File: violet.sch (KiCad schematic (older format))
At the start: 38 parts, among them J1 NEIGHBOR1, J2 NEIGHBOR2, J3 NEIGHBOR1, J4 BONUS_ROW, J5 NEIGHBOR2, J6 NEIGHBOR1, J7 BONUS_ROW, J8 BONUS_ROW, J9 NEIGHBOR2, U1 PCA9698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

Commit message: Remove U3 & U4; re-label signals; set up U5; fix U1 &U2 I2C addresses; fix minor errors
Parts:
- removed C10: C, symbol Device:C
- removed C9: 100nF, gsg-modules:0603, symbol Device:C
- removed U3: PCA9674, gsg-modules:TSSOP16, symbol gsg-symbols:PCA9674
- removed U4: 74HC4051, symbol 74xx:74HC4051
- C7, C8: value C -> 1uF; Description (none) -> CAP CER 1UF 10V X5R 0603; Manufacturer (none) -> Samsung Electro-Mechanics; Part Number (none) -> CL10A105KP8NNNC
- R10: value R -> 0.1; footprint (none) -> gsg-modules:0603; Description (none) -> RES 0.1 OHM 1% 1/10W 0603; Manufacturer (none) -> Panasonic Electronic Components; Part Number (none) -> ERJ-3RSFR10V
- R8: value R -> 12k; footprint (none) -> gsg-modules:0603; Description (none) -> RES 12K OHM 1% 1/10W 0603; Manufacturer (none) -> Stackpole; Part Number (none) -> RMCF0603FT12K0
- R9: value R -> 43.2k; footprint (none) -> gsg-modules:0603; Description (none) -> RES SMD 43.2K OHM 1% 1/10W 0603; Manufacturer (none) -> Yageo; Part Number (none) -> RC0603FR-0743K2L
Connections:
- net EUT_5V is gone; now on net ADC0_5: U5.6 (VOUT)
- net U3_IO_P0 is gone; now on net U1_IO2_7: J5.30 (Pin_30)
- net U3_IO_P1 is gone; now on net U1_IO2_6: J5.32 (Pin_32)
- net U3_IO_P2 is gone; now on net U1_IO2_5: J5.38 (Pin_38)
- net U3_IO_P3 is gone; now on net U1_IO2_3: J4.11 (Pin_11)
- net U3_IO_P4 is gone; now on net U1_IO2_4: J5.2 (Pin_2)
- net +5V: no longer C8.1, U5.1 (VIN)
- net ADC0_2: now also J3.2 (Pin_2), R10.1; no longer J4.5 (Pin_5), J8.5 (Pin_5)
- net ADC0_5: now also C7.1, R10.2; no longer J4.4 (Pin_4), J8.4 (Pin_4)
- net EUT_P1_10: now also J3.20 (Pin_20)
- net EUT_P1_11: now also J3.22 (Pin_22)
- net EUT_P1_12: now also J3.21 (Pin_21)
- net EUT_P1_13: now also J3.26 (Pin_26)
- net EUT_P1_14: now also J3.25 (Pin_25)
- net EUT_P1_7: now also J3.15 (Pin_15)
- net EUT_P1_8: now also J3.18 (Pin_18)
- net EUT_P1_9: now also J3.17 (Pin_17)
- net GND: now also C7.2, R7.2; no longer C7.1, R8.2
- net I2C0_SCL: now also U1.28 (AD1), U2.28 (AD1); no longer J5.40 (Pin_40), J9.40 (Pin_40)
- net I2C0_SDA: no longer J5.39 (Pin_39), J9.39 (Pin_39)
- net P1_15: no longer R7.2
- net P1_5: no longer J6.13 (Pin_13)
- net P1_6: no longer J6.16 (Pin_16)
- net P2_3: no longer J9.20 (Pin_20)
- net P2_5: no longer J9.18 (Pin_18)
- net P4_2: now also R7.1; no longer J9.8 (Pin_8), R8.1
- net P4_6: now also R8.2; no longer R10.2
- net P5_0: no longer J6.8 (Pin_8)
- net P5_2: no longer J6.14 (Pin_14)
- net P5_3: no longer J6.19 (Pin_19)
- net P5_4: no longer J6.24 (Pin_24)
- net P5_5: no longer J6.23 (Pin_23)
- net P5_6: no longer J6.27 (Pin_27)
- net P6_8: no longer J9.29 (Pin_29)
- net P7_0: no longer J9.27 (Pin_27)
- net U1_IO0_2: no longer U1.5 (IO0_2)
- net U1_IO2_3: no longer J3.27 (Pin_27)
- net U1_IO2_4: no longer J3.26 (Pin_26)
- net U1_IO2_5: no longer J3.25 (Pin_25)
- net U1_IO2_6: no longer J3.24 (Pin_24)
- net U1_IO2_7: no longer J3.23 (Pin_23)
- net VCC: now also C8.1, R8.1, U5.1 (VIN); no longer C7.2, J3.2 (Pin_2), J6.2 (Pin_2), R10.1, R7.1, U1.28 (AD1), U2.28 (AD1)
- removed net U1_IO3_0: J3.22 (Pin_22), U1.36 (IO3_0), U2.36 (IO3_0)
- net U1_IO3_1: no longer names the net of U1.37 (IO3_1)
- net U1_IO3_1: no longer J3.21 (Pin_21)
- net U1_IO3_2: no longer names the net of U1.38 (IO3_2)
- net U1_IO3_2: no longer J3.20 (Pin_20)
- net U1_IO3_3: no longer names the net of U1.40 (IO3_3)
- net U1_IO3_3: no longer J3.19 (Pin_19)
- net U1_IO3_4: no longer names the net of U1.41 (IO3_4)
- net U1_IO3_4: no longer J3.18 (Pin_18)
- net U1_IO3_5: no longer names the net of U1.42 (IO3_5)
- net U1_IO3_5: no longer J3.17 (Pin_17)
- net U1_IO3_6: no longer names the net of U1.43 (IO3_6)
- net U1_IO3_6: no longer J3.16 (Pin_16)
- net U1_IO3_7: no longer names the net of U1.44 (IO3_7)
- net U1_IO3_7: no longer J3.15 (Pin_15)
- net U1_IO4_0: no longer names the net of U1.45 (IO4_0)
- net U1_IO4_0: no longer J3.14 (Pin_14)
- net U1_IO4_1: no longer names the net of U1.47 (IO4_1)
- net U1_IO4_1: no longer J3.13 (Pin_13)
- net U1_IO4_5: no longer names the net of U1.52 (IO4_5)
- net U1_IO4_5: no longer J3.8 (Pin_8)
- net U2_IO3_0 renamed EUT_P4_2
- net EUT_P4_2: now also J9.8 (Pin_8)
- net U2_IO4_0: no longer names the net of U2.45 (IO4_0)
- net U2_IO4_0: no longer J5.18 (Pin_18)
- net U2_IO4_2: no longer names the net of U2.48 (IO4_2)
- net U2_IO4_2: no longer J5.20 (Pin_20)
- net U2_IO4_6: no longer names the net of U2.53 (IO4_6)
- net U2_IO4_6: no longer J5.27 (Pin_27)
- net U2_IO4_7: no longer names the net of U2.54 (IO4_7)
- net U2_IO4_7: no longer J5.29 (Pin_29)
- new net EUT_ADC0_2: J4.5 (Pin_5), J8.5 (Pin_5)
- new net EUT_ADC0_5: J4.4 (Pin_4), J8.4 (Pin_4)
- new net EUT_I2C0_SCL: J5.40 (Pin_40), J9.40 (Pin_40)
- new net EUT_I2C0_SDA: J5.39 (Pin_39), J9.39 (Pin_39)
- new net EUT_P1_5: J3.13 (Pin_13), J6.13 (Pin_13)
- new net EUT_P1_6: J3.16 (Pin_16), J6.16 (Pin_16)
- new net EUT_P2_3: J5.20 (Pin_20), J9.20 (Pin_20)
- new net EUT_P2_5: J5.18 (Pin_18), J9.18 (Pin_18)
- new net EUT_P5_0: J3.8 (Pin_8), J6.8 (Pin_8)
- new net EUT_P5_2: J3.14 (Pin_14), J6.14 (Pin_14)
- new net EUT_P5_3: J3.19 (Pin_19), J6.19 (Pin_19)
- new net EUT_P5_4: J3.24 (Pin_24), J6.24 (Pin_24)
- new net EUT_P5_5: J3.23 (Pin_23), J6.23 (Pin_23)
- new net EUT_P5_6: J3.27 (Pin_27), J6.27 (Pin_27)
- new net EUT_P6_8: J5.29 (Pin_29), J9.29 (Pin_29)
- new net EUT_P7_0: J5.27 (Pin_27), J9.27 (Pin_27)
- no-connect marks 168 -> 162
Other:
- note added: "Address: 0x10"
- note added: "Address: 0x11"
- note added: "Plug Gladiolus/Azalea testing unit in here."
- note removed: "???"
- note removed: "Plug Gladiolus testing unit in here."
- moved on the sheet: C8, R9, U5

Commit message: Add remaining footprints
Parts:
- added J10: Conn_01x08, gsg-modules:HEADER-1x8, symbol Connector_Generic:Conn_01x08
- C7, C8: footprint (none) -> gsg-modules:0603
- J1, J2, J3, J5, J6, J9: footprint neighbor:HEADER-2x20 -> gsg-modules:HEADER-2x20
- J4, J7, J8: footprint neighbor:HEADER-1x20 -> gsg-modules:HEADER-1x20
- U5: footprint (none) -> gsg-modules:SOT457
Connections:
- no-connect marks 162 -> 170
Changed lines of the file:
@@
 F 0 "J2" H 15500 2900 50  0000 C CNN
 F 1 "NEIGHBOR2" V 15500 1850 50  0000 C CNN
-F 2 "neighbor:HEADER-2x20" H 15450 900 60  0001 C CNN
+F 2 "gsg-modules:HEADER-2x20" H 15450 900 60  0001 C CNN
 F 3 "" H 15450 900 60  0000 C CNN
 F 4 "Adam Tech" H 15450 1850 60  0001 C CNN "Manufacturer"
@@
 F 0 "J1" H 13800 2900 50  0000 C CNN
 F 1 "NEIGHBOR1" V 13800 1850 50  0000 C CNN
-F 2 "neighbor:HEADER-2x20" H 13750 900 60  0001 C CNN
+F 2 "gsg-modules:HEADER-2x20" H 13750 900 60  0001 C CNN
 F 3 "" H 13750 900 60  0000 C CNN
 F 4 "Adam Tech" H 13750 1850 60  0001 C CNN "Manufacturer"
@@
 F 0 "J7" H 14600 4300 50  0000 C CNN
 F 1 "BONUS_ROW" V 14700 3250 50  0000 C CNN
-F 2 "neighbor:HEADER-1x20" H 14600 3250 60  0001 C CNN
+F 2 "gsg-modules:HEADER-1x20" H 14600 3250 60  0001 C CNN
 F 3 "" H 14600 3250 60  0000 C CNN
 F 4 "Samtec" H 14600 3250 60  0001 C CNN "Manufacturer"
@@
 F 0 "J5" H 3850 3400 50  0000 C CNN
 F 1 "NEIGHBOR2" V 3850 2350 50  0000 C CNN
-F 2 "neighbor:HEADER-2x20" H 3800 1400 60  0001 C CNN
+F 2 "gsg-modules:HEADER-2x20" H 3800 1400 60  0001 C CNN
 F 3 "" H 3800 1400 60  0000 C CNN
 F 4 "Adam Tech" H 3800 2350 60  0001 C CNN "Manufacturer"
@@
 F 0 "J3" H 2150 3400 50  0000 C CNN
 F 1 "NEIGHBOR1" V 2150 2350 50  0000 C CNN
-F 2 "neighbor:HEADER-2x20" H 2100 1400 60  0001 C CNN
+F 2 "gsg-modules:HEADER-2x20" H 2100 1400 60  0001 C CNN
 F 3 "" H 2100 1400 60  0000 C CNN
 F 4 "Adam Tech" H 2100 2350 60  0001 C CNN "Manufacturer"
@@
 F 0 "J4" H 2950 4800 50  0000 C CNN
 F 1 "BONUS_ROW" V 3050 3750 50  0000 C CNN
-F 2 "neighbor:HEADER-1x20" H 2950 3750 60  0001 C CNN
+F 2 "gsg-modules:HEADER-1x20" H 2950 3750 60  0001 C CNN
 F 3 "" H 2950 3750 60  0000 C CNN
 F 4 "Samtec" H 2950 3750 60  0001 C CNN "Manufacturer"
@@
 F 0 "U5" H 7500 7337 60  0000 C CNN
 F 1 "AP2553W6-7" H 7500 7231 60  0000 C CNN
-F 2 "" H 7500 6950 60  0000 C CNN
+F 2 "gsg-modules:SOT457" H 7500 6950 60  0001 C CNN
 F 3 "" H 7500 6950 60  0000 C CNN
 	1    7500 6950
@@
 F 0 "C8" H 6365 7096 50  0000 L CNN
 F 1 "1uF" H 6365 7005 50  0000 L CNN
-F 2 "" H 6288 6900 50  0001 C CNN
+F 2 "gsg-modules:0603" H 6288 6900 50  0001 C CNN
 F 3 "~" H 6250 7050 50  0001 C CNN
 F 4 "Samsung Electro-Mechanics" H 6250 7050 50  0001 C CNN "Manufacturer"
@@
 F 0 "J9" H 15550 8050 50  0000 C CNN
 F 1 "NEIGHBOR2" V 15550 7000 50  0000 C CNN
-F 2 "neighbor:HEADER-2x20" H 15500 6050 60  0001 C CNN
+F 2 "gsg-modules:HEADER-2x20" H 15500 6050 60  0001 C CNN
 F 3 "" H 15500 6050 60  0000 C CNN
 F 4 "Adam Tech" H 15500 7000 60  0001 C CNN "Manufacturer"
@@
 F 0 "J6" H 13850 8050 50  0000 C CNN
 F 1 "NEIGHBOR1" V 13850 7000 50  0000 C CNN
-F 2 "neighbor:HEADER-2x20" H 13800 6050 60  0001 C CNN
+F 2 "gsg-modules:HEADER-2x20" H 13800 6050 60  0001 C CNN
 F 3 "" H 13800 6050 60  0000 C CNN
 F 4 "Adam Tech" H 13800 7000 60  0001 C CNN "Manufacturer"
@@
 F 0 "J8" H 14050 9400 50  0000 C CNN
 F 1 "BONUS_ROW" V 14150 8350 50  0000 C CNN
-F 2 "neighbor:HEADER-1x20" H 14050 8350 60  0001 C CNN
+F 2 "gsg-modules:HEADER-1x20" H 14050 8350 60  0001 C CNN
 F 3 "" H 14050 8350 60  0000 C CNN
 F 4 "Samtec" H 14050 8350 60  0001 C CNN "Manufacturer"
@@
 F 0 "C7" H 9015 7146 50  0000 L CNN
 F 1 "1uF" H 9015 7055 50  0000 L CNN
-F 2 "" H 8938 6950 50  0001 C CNN
+F 2 "gsg-modules:0603" H 8938 6950 50  0001 C CNN
 F 3 "~" H 8900 7100 50  0001 C CNN
 F 4 "Samsung Electro-Mechanics" H 8900 7100 50  0001 C CNN "Manufacturer"
@@
 NoConn ~ 5600 1950
 NoConn ~ 14250 2250
+$Comp
+L Connector_Generic:Conn_01x08 J10
+U 1 1 605A089F
+P 2050 6150
+F 0 "J10" H 2130 6142 50  0000 L CNN
+F 1 "Conn_01x08" H 2130 6051 50  0000 L CNN
+F 2 "gsg-modules:HEADER-1x8" H 2050 6150 50  0001 C CNN
+F 3 "~" H 2050 6150 50  0001 C CNN
+F 4 "Samtec Inc." H 2050 6150 50  0001 C CNN "Manufacturer"
+F 5 "SSQ-108-01-G-S" H 2050 6150 50  0001 C CNN "Part Number"
+F 6 "CONN RCPT 8POS 0.1 GOLD PCB" H 2050 6150 50  0001 C CNN "Description"
+	1    2050 6150
+	1    0    0    -1
+$EndComp
+NoConn ~ 1850 5850
+NoConn ~ 1850 5950
+NoConn ~ 1850 6050
+NoConn ~ 1850 6150
+NoConn ~ 1850 6250
+NoConn ~ 1850 6350
+NoConn ~ 1850 6450
+NoConn ~ 1850 6550
 $EndSCHEMATC

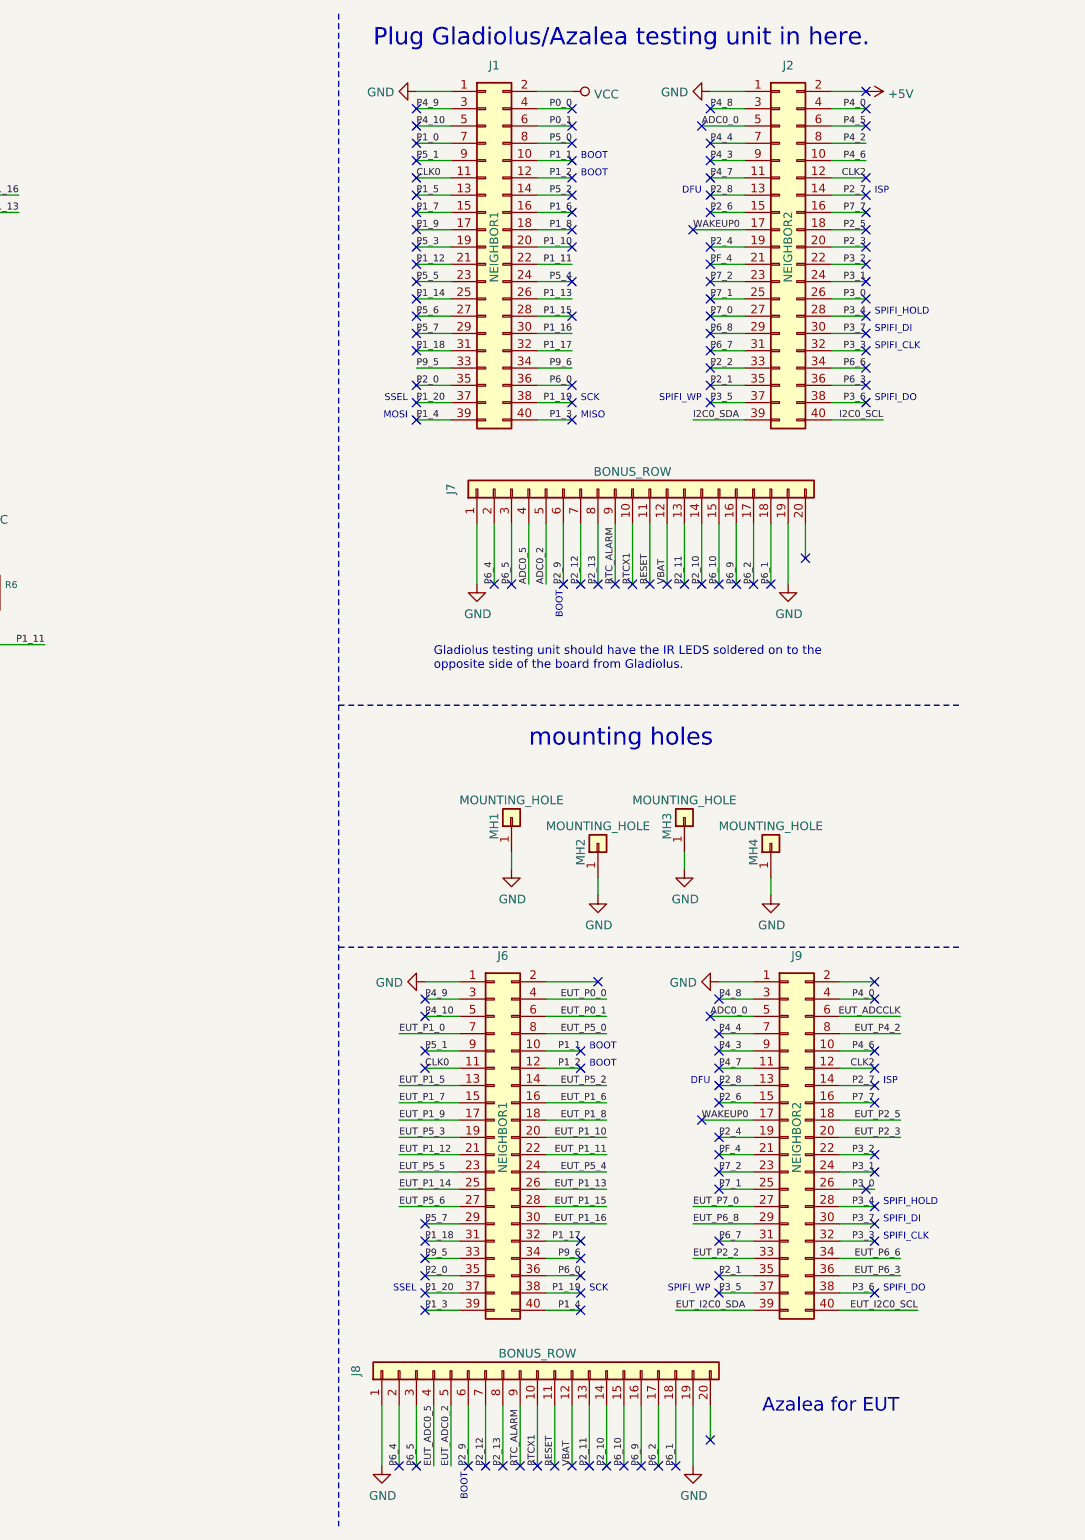
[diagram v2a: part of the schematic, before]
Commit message: Add more mounting holes
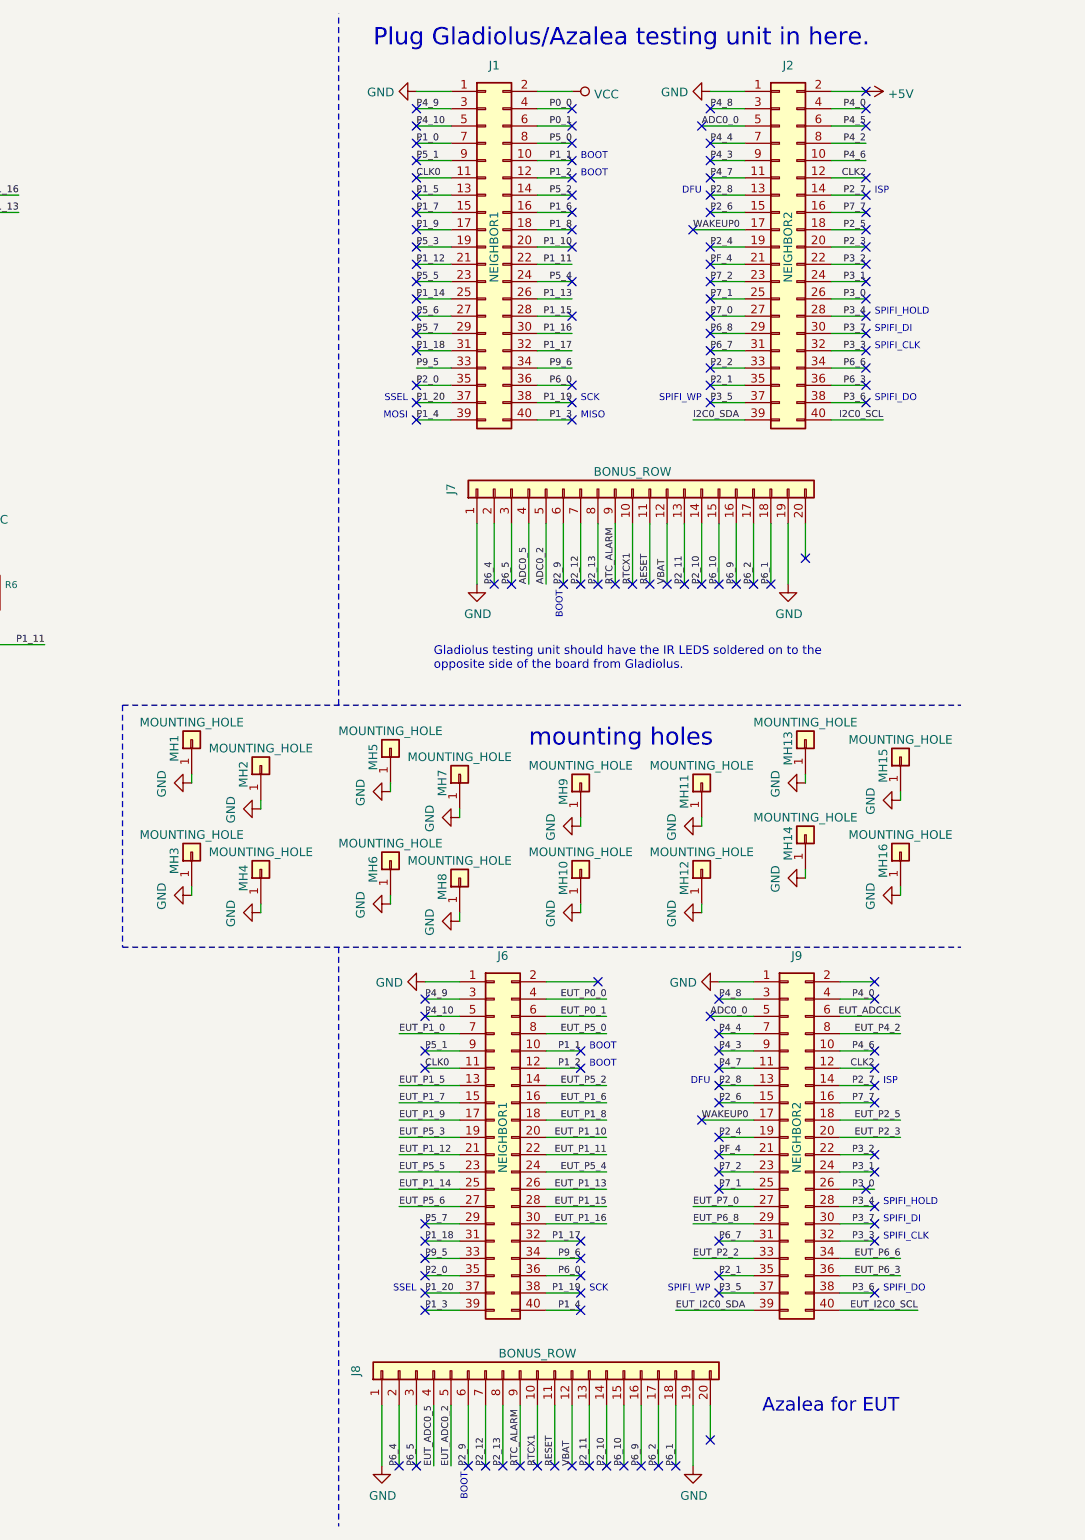
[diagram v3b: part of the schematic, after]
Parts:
- added MH10, MH11, MH12, MH13, MH14, MH15, MH16, MH5, MH6, MH7, MH8, MH9: MOUNTING_HOLE, neighbor:HOLE126MIL-COPPER, symbol Connector_Generic:Conn_01x01
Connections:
- net GND: now also MH10.1 (Pin_1), MH11.1 (Pin_1), MH12.1 (Pin_1), MH13.1 (Pin_1), MH14.1 (Pin_1), MH15.1 (Pin_1), MH16.1 (Pin_1), MH5.1 (Pin_1), MH6.1 (Pin_1), MH7.1 (Pin_1), MH8.1 (Pin_1), MH9.1 (Pin_1)
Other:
- moved on the sheet: MH1, MH2, MH3, MH4

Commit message: Fix mounting hole footprints
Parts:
- MH1, MH10, MH11, MH12, MH13, MH14, MH15, MH16, MH2, MH3, MH4, MH5, MH6, MH7, MH8, MH9: footprint neighbor:HOLE126MIL-COPPER -> gsg-modules:HOLE126MIL-COPPER
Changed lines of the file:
@@
 F 0 "MH3" H 12000 5450 50  0000 C CNN
 F 1 "MOUNTING_HOLE" V 12150 5350 50  0000 C CNN
-F 2 "neighbor:HOLE126MIL-COPPER" H 12050 5350 60  0001 C CNN
+F 2 "gsg-modules:HOLE126MIL-COPPER" H 12050 5350 60  0001 C CNN
 F 3 "" H 12050 5350 60  0000 C CNN
 F 4 "DNP" H 12050 5350 60  0001 C CNN "Note"
@@
 F 0 "MH4" H 12400 5550 50  0000 C CNN
 F 1 "MOUNTING_HOLE" V 12550 5450 50  0000 C CNN
-F 2 "neighbor:HOLE126MIL-COPPER" H 12450 5450 60  0001 C CNN
+F 2 "gsg-modules:HOLE126MIL-COPPER" H 12450 5450 60  0001 C CNN
 F 3 "" H 12450 5450 60  0000 C CNN
 F 4 "DNP" H 12450 5450 60  0001 C CNN "Note"
@@
 F 0 "MH1" H 12000 4800 50  0000 C CNN
 F 1 "MOUNTING_HOLE" V 12150 4700 50  0000 C CNN
-F 2 "neighbor:HOLE126MIL-COPPER" H 12050 4700 60  0001 C CNN
+F 2 "gsg-modules:HOLE126MIL-COPPER" H 12050 4700 60  0001 C CNN
 F 3 "" H 12050 4700 60  0000 C CNN
 F 4 "DNP" H 12050 4700 60  0001 C CNN "Note"
@@
 F 0 "MH2" H 12400 4950 50  0000 C CNN
 F 1 "MOUNTING_HOLE" V 12550 4850 50  0000 C CNN
-F 2 "neighbor:HOLE126MIL-COPPER" H 12450 4850 60  0001 C CNN
+F 2 "gsg-modules:HOLE126MIL-COPPER" H 12450 4850 60  0001 C CNN
 F 3 "" H 12450 4850 60  0000 C CNN
 F 4 "DNP" H 12450 4850 60  0001 C CNN "Note"
@@
 F 0 "MH9" H 14250 5050 50  0000 C CNN
 F 1 "MOUNTING_HOLE" V 14400 4950 50  0000 C CNN
-F 2 "neighbor:HOLE126MIL-COPPER" H 14300 4950 60  0001 C CNN
+F 2 "gsg-modules:HOLE126MIL-COPPER" H 14300 4950 60  0001 C CNN
 F 3 "" H 14300 4950 60  0000 C CNN
 F 4 "DNP" H 14300 4950 60  0001 C CNN "Note"
@@
 F 0 "MH10" H 14250 5550 50  0000 C CNN
 F 1 "MOUNTING_HOLE" V 14400 5450 50  0000 C CNN
-F 2 "neighbor:HOLE126MIL-COPPER" H 14300 5450 60  0001 C CNN
+F 2 "gsg-modules:HOLE126MIL-COPPER" H 14300 5450 60  0001 C CNN
 F 3 "" H 14300 5450 60  0000 C CNN
 F 4 "DNP" H 14300 5450 60  0001 C CNN "Note"
@@
 F 0 "MH11" H 14950 5050 50  0000 C CNN
 F 1 "MOUNTING_HOLE" V 15100 4950 50  0000 C CNN
-F 2 "neighbor:HOLE126MIL-COPPER" H 15000 4950 60  0001 C CNN
+F 2 "gsg-modules:HOLE126MIL-COPPER" H 15000 4950 60  0001 C CNN
 F 3 "" H 15000 4950 60  0000 C CNN
 F 4 "DNP" H 15000 4950 60  0001 C CNN "Note"
@@
 F 0 "MH12" H 14950 5550 50  0000 C CNN
 F 1 "MOUNTING_HOLE" V 15100 5450 50  0000 C CNN
-F 2 "neighbor:HOLE126MIL-COPPER" H 15000 5450 60  0001 C CNN
+F 2 "gsg-modules:HOLE126MIL-COPPER" H 15000 5450 60  0001 C CNN
 F 3 "" H 15000 5450 60  0000 C CNN
 F 4 "DNP" H 15000 5450 60  0001 C CNN "Note"
@@
 F 0 "MH13" H 15550 4800 50  0000 C CNN
 F 1 "MOUNTING_HOLE" V 15700 4700 50  0000 C CNN
-F 2 "neighbor:HOLE126MIL-COPPER" H 15600 4700 60  0001 C CNN
+F 2 "gsg-modules:HOLE126MIL-COPPER" H 15600 4700 60  0001 C CNN
 F 3 "" H 15600 4700 60  0000 C CNN
 F 4 "DNP" H 15600 4700 60  0001 C CNN "Note"
@@
 F 0 "MH14" H 15550 5350 50  0000 C CNN
 F 1 "MOUNTING_HOLE" V 15700 5250 50  0000 C CNN
-F 2 "neighbor:HOLE126MIL-COPPER" H 15600 5250 60  0001 C CNN
+F 2 "gsg-modules:HOLE126MIL-COPPER" H 15600 5250 60  0001 C CNN
 F 3 "" H 15600 5250 60  0000 C CNN
 F 4 "DNP" H 15600 5250 60  0001 C CNN "Note"
@@
 F 0 "MH15" H 16100 4900 50  0000 C CNN
 F 1 "MOUNTING_HOLE" V 16250 4800 50  0000 C CNN
-F 2 "neighbor:HOLE126MIL-COPPER" H 16150 4800 60  0001 C CNN
+F 2 "gsg-modules:HOLE126MIL-COPPER" H 16150 4800 60  0001 C CNN
 F 3 "" H 16150 4800 60  0000 C CNN
 F 4 "DNP" H 16150 4800 60  0001 C CNN "Note"
@@
 F 0 "MH16" H 16100 5450 50  0000 C CNN
 F 1 "MOUNTING_HOLE" V 16250 5350 50  0000 C CNN
-F 2 "neighbor:HOLE126MIL-COPPER" H 16150 5350 60  0001 C CNN
+F 2 "gsg-modules:HOLE126MIL-COPPER" H 16150 5350 60  0001 C CNN
 F 3 "" H 16150 5350 60  0000 C CNN
 F 4 "DNP" H 16150 5350 60  0001 C CNN "Note"
@@
 F 0 "MH6" H 13150 5500 50  0000 C CNN
 F 1 "MOUNTING_HOLE" V 13300 5400 50  0000 C CNN
-F 2 "neighbor:HOLE126MIL-COPPER" H 13200 5400 60  0001 C CNN
+F 2 "gsg-modules:HOLE126MIL-COPPER" H 13200 5400 60  0001 C CNN
 F 3 "" H 13200 5400 60  0000 C CNN
 F 4 "DNP" H 13200 5400 60  0001 C CNN "Note"
@@
 F 0 "MH8" H 13550 5600 50  0000 C CNN
 F 1 "MOUNTING_HOLE" V 13700 5500 50  0000 C CNN
-F 2 "neighbor:HOLE126MIL-COPPER" H 13600 5500 60  0001 C CNN
+F 2 "gsg-modules:HOLE126MIL-COPPER" H 13600 5500 60  0001 C CNN
 F 3 "" H 13600 5500 60  0000 C CNN
 F 4 "DNP" H 13600 5500 60  0001 C CNN "Note"
@@
 F 0 "MH5" H 13150 4850 50  0000 C CNN
 F 1 "MOUNTING_HOLE" V 13300 4750 50  0000 C CNN
-F 2 "neighbor:HOLE126MIL-COPPER" H 13200 4750 60  0001 C CNN
+F 2 "gsg-modules:HOLE126MIL-COPPER" H 13200 4750 60  0001 C CNN
 F 3 "" H 13200 4750 60  0000 C CNN
 F 4 "DNP" H 13200 4750 60  0001 C CNN "Note"
@@
 F 0 "MH7" H 13550 5000 50  0000 C CNN
 F 1 "MOUNTING_HOLE" V 13700 4900 50  0000 C CNN
-F 2 "neighbor:HOLE126MIL-COPPER" H 13600 4900 60  0001 C CNN
+F 2 "gsg-modules:HOLE126MIL-COPPER" H 13600 4900 60  0001 C CNN
 F 3 "" H 13600 4900 60  0000 C CNN
 F 4 "DNP" H 13600 4900 60  0001 C CNN "Note"
